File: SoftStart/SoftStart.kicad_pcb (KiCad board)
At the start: 2 copper layers, 88 x 56 mm, 31 parts, among them J1 LIVE, J10 LIVE, J11 Conn_01x02, J2 NEUTRAL, J3 SW1, J4 SW2, J5 NEUTRAL, J6 SWOUTPUT, J7 LIVE, J8 LIVE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

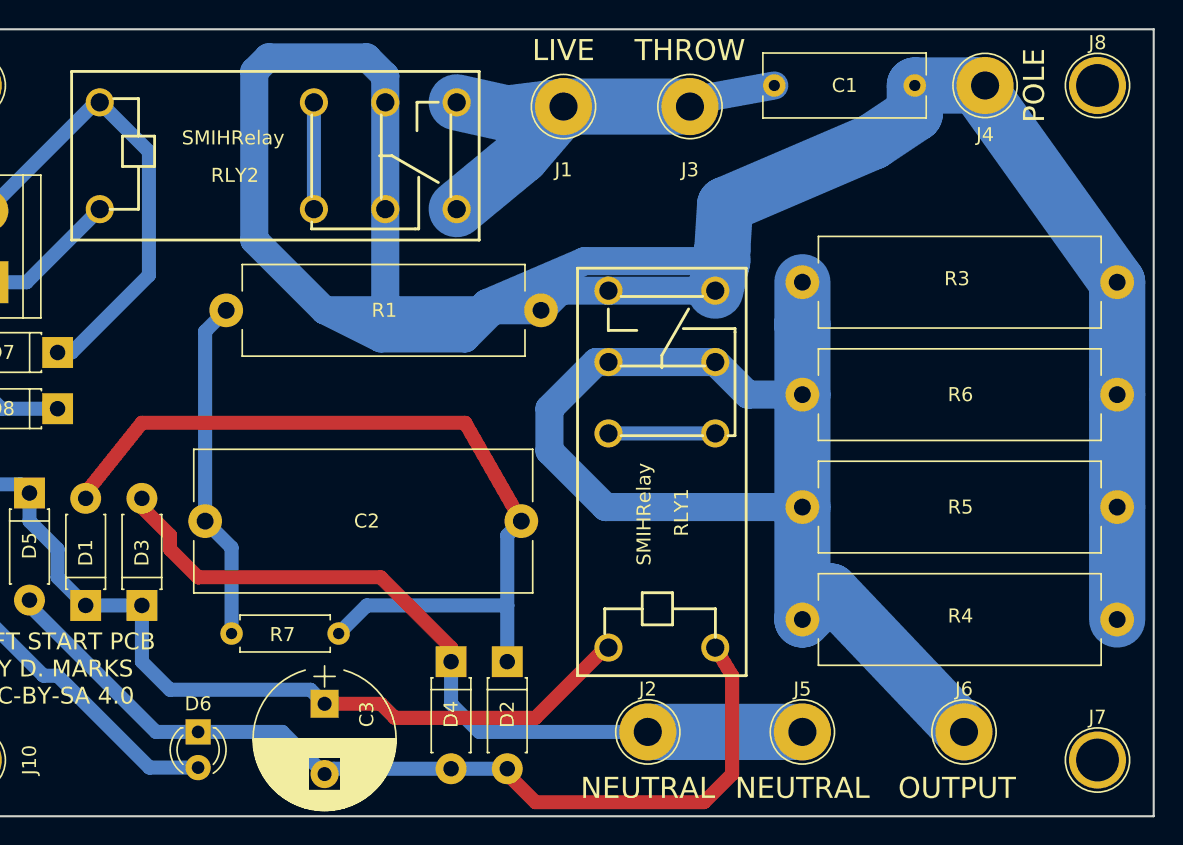
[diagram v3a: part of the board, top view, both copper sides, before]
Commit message: Changed to 2N5551/2N5401 from BC546C/BC556C transistors
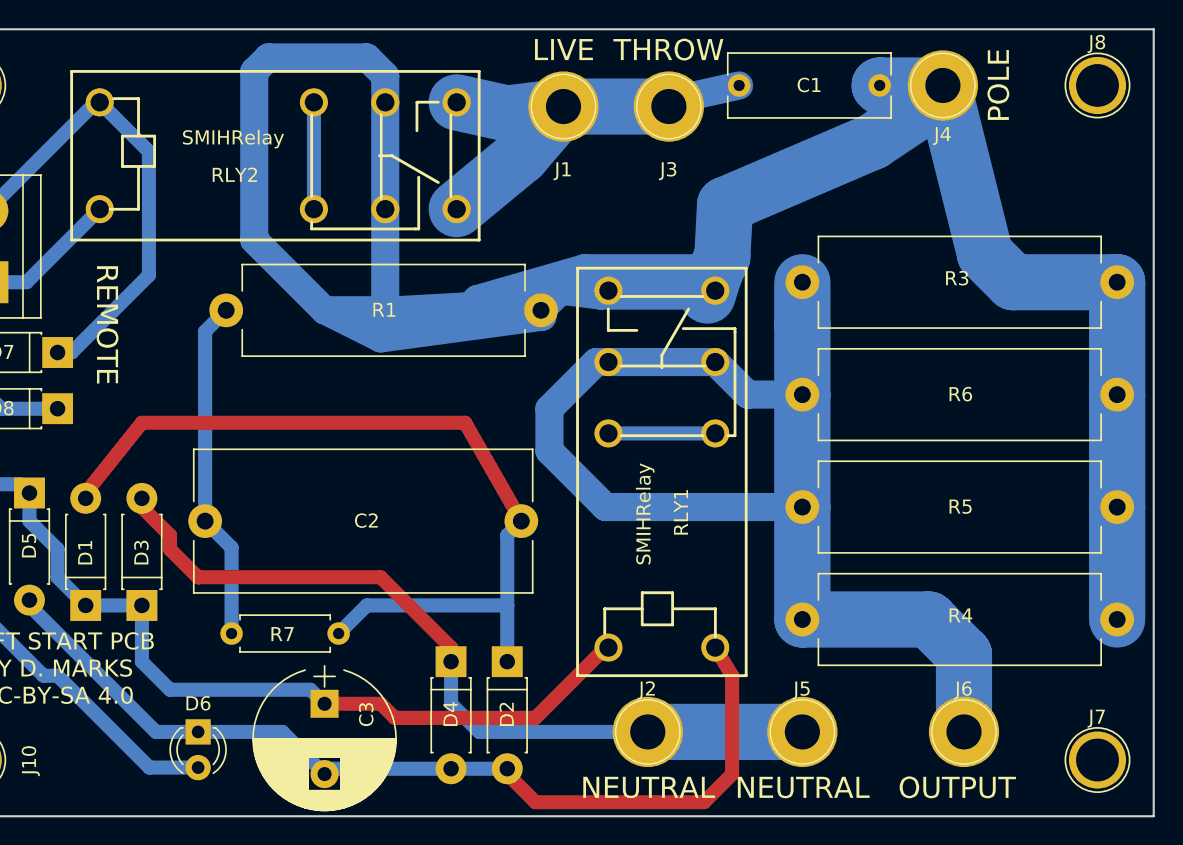
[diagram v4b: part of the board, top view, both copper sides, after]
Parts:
- moved J4 3.00 mm to (193.0, 73.0)
- moved C1 2.50 mm to (188.5, 73.0)
- moved J3 1.50 mm to (173.5, 74.5)
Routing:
- net Net-(C1-Pad1): track 179.0 -> 192.0 mm
- net Net-(C1-Pad2): track 33.6 -> 31.1 mm
- net Net-(J6-Pad1): track 83.6 -> 85.0 mm
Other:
- board text added: "REMOTE"
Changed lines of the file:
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@@
     (links 46)
     (no_connects 0)
-    (area 119.924999 68.924999 208.075001 125.075001)
+    (area 119.924999 68.465 208.075001 125.075001)
     (thickness 1.6)
-    (drawings 11)
-    (tracks 131)
+    (drawings 12)
+    (tracks 134)
     (zones 0)
     (modules 31)
@@
   )
   (setup
-    (last_trace_width 0.25)
+    (last_trace_width 2)
     (user_trace_width 0.5)
     (user_trace_width 1)
@@
     (mod_text_size 1 1)
     (mod_text_width 0.15)
-    (pad_size 4.064 4.064)
-    (pad_drill 2)
+    (pad_size 5 5)
+    (pad_drill 2.5)
     (pad_to_mask_clearance 0.2)
     (aux_axis_origin 0 0)
@@
   )
   (module Capacitors_THT:C_Rect_L11.5mm_W4.5mm_P10.00mm_MKT (layer F.Cu)
-    (at 191 73 180)
+    (at 188.5 73 180)
     (descr "C, Rect series, Radial, pin pitch=10.00mm, , length*width=11.5*4.5mm^2, Capacitor, https://en.tdk.eu/inf/20/20/db/fc_2009/MKT_B32560_564.pdf")
     (tags "C Rect series Radial pin pitch 10.00mm  length 11.5mm width 4.5mm Capacitor")
@@
     (fp_circle (center 0 0) (end 2.6 0) (layer F.CrtYd) (width 0.05))
     (fp_circle (center 0 0) (end 0 -2.286) (layer F.SilkS) (width 0.12))
-    (pad 1 thru_hole circle (at 0 0) (size 4.064 4.064) (drill 2) (layers *.Cu *.Mask)
+    (pad 1 thru_hole circle (at 0 0) (size 5 5) (drill 2.5) (layers *.Cu *.Mask)
       (net 2 "Net-(C1-Pad2)"))
   )
@@
     (fp_circle (center 0 0) (end 2.6 0) (layer F.CrtYd) (width 0.05))
     (fp_circle (center 0 0) (end 0 -2.286) (layer F.SilkS) (width 0.12))
-    (pad 1 thru_hole circle (at 0 0) (size 4.064 4.064) (drill 2) (layers *.Cu *.Mask)
+    (pad 1 thru_hole circle (at 0 0) (size 5 5) (drill 2.5) (layers *.Cu *.Mask)
       (net 7 "Net-(D3-Pad2)"))
   )
   (module Connectors:1pin (layer F.Cu)
-    (at 175 74.5)
+    (at 173.5 74.5)
     (descr "module 1 pin (ou trou mecanique de percage)")
     (tags DEV)
@@
     (fp_circle (center 0 0) (end 2.6 0) (layer F.CrtYd) (width 0.05))
     (fp_circle (center 0 0) (end 0 -2.286) (layer F.SilkS) (width 0.12))
-    (pad 1 thru_hole circle (at 0 0) (size 4.064 4.064) (drill 2) (layers *.Cu *.Mask)
+    (pad 1 thru_hole circle (at 0 0) (size 5 5) (drill 2.5) (layers *.Cu *.Mask)
       (net 2 "Net-(C1-Pad2)"))
   )
   (module Connectors:1pin (layer F.Cu)
-    (at 196 73)
+    (at 193 73)
     (descr "module 1 pin (ou trou mecanique de percage)")
     (tags DEV)
@@
     (fp_circle (center 0 0) (end 2.6 0) (layer F.CrtYd) (width 0.05))
     (fp_circle (center 0 0) (end 0 -2.286) (layer F.SilkS) (width 0.12))
-    (pad 1 thru_hole circle (at 0 0) (size 4.064 4.064) (drill 2) (layers *.Cu *.Mask)
+    (pad 1 thru_hole circle (at 0 0) (size 5 5) (drill 2.5) (layers *.Cu *.Mask)
       (net 1 "Net-(C1-Pad1)"))
   )
@@
     (fp_circle (center 0 0) (end 2.6 0) (layer F.CrtYd) (width 0.05))
     (fp_circle (center 0 0) (end 0 -2.286) (layer F.SilkS) (width 0.12))
-    (pad 1 thru_hole circle (at 0 0) (size 4.064 4.064) (drill 2) (layers *.Cu *.Mask)
+    (pad 1 thru_hole circle (at 0 0) (size 5 5) (drill 2.5) (layers *.Cu *.Mask)
       (net 7 "Net-(D3-Pad2)"))
   )
@@
     (fp_circle (center 0 0) (end 2.6 0) (layer F.CrtYd) (width 0.05))
     (fp_circle (center 0 0) (end 0 -2.286) (layer F.SilkS) (width 0.12))
-    (pad 1 thru_hole circle (at 0 0) (size 4.064 4.064) (drill 2) (layers *.Cu *.Mask)
+    (pad 1 thru_hole circle (at 0 0) (size 5 5) (drill 2.5) (layers *.Cu *.Mask)
       (net 9 "Net-(J6-Pad1)"))
   )
@@
       (net 2 "Net-(C1-Pad2)"))
   )
+  (gr_text REMOTE (at 133.5 90 270) (layer F.SilkS)
+    (effects (font (size 1.5 1.5) (thickness 0.3)))
+  )
   (gr_text "SOFT START PCB\nBY D. MARKS\nCC-BY-SA 4.0" (at 130 114.5) (layer F.SilkS)
     (effects (font (size 1.2 1.2) (thickness 0.2)))
@@
   (gr_line (start 208 69) (end 208 125) (angle 90) (layer Edge.Cuts) (width 0.15))
   (gr_line (start 120 69) (end 208 69) (angle 90) (layer Edge.Cuts) (width 0.15))
-  (gr_text POLE (at 199.5 73 90) (layer F.SilkS)
+  (gr_text POLE (at 197 73 90) (layer F.SilkS)
     (effects (font (size 1.5 1.5) (thickness 0.3)))
   )
-  (gr_text THROW (at 175 70.5) (layer F.SilkS)
+  (gr_text THROW (at 173.5 70.5) (layer F.SilkS)
     (effects (font (size 1.5 1.5) (thickness 0.3)))
   )
@@
     (effects (font (size 1.5 1.5) (thickness 0.3)))
   )
-  (segment (start 164.4 89) (end 161.5 88.5) (width 2) (layer B.Cu) (net 1))
+  (segment (start 205.4 87) (end 198 87) (width 4) (layer B.Cu) (net 1))
+  (segment (start 196 85) (end 193 73) (width 4) (layer B.Cu) (net 1) (status 20))
+  (segment (start 198 87) (end 196 85) (width 4) (layer B.Cu) (net 1))
+  (segment (start 164.4 89) (end 160.85 88.2) (width 2) (layer B.Cu) (net 1))
   (segment (start 153 91) (end 149 89) (width 2) (layer B.Cu) (net 1))
-  (segment (start 159 91) (end 153 91) (width 2) (layer B.Cu) (net 1))
-  (segment (start 161.5 88.5) (end 159 91) (width 2) (layer B.Cu) (net 1))
-  (segment (start 169.2 87.6) (end 176.8 87.6) (width 2) (layer B.Cu) (net 1))
+  (segment (start 164.5 89.45) (end 153 91) (width 2) (layer B.Cu) (net 1))
+  (segment (start 160.85 88.2) (end 164.5 89.45) (width 2) (layer B.Cu) (net 1))
+  (segment (start 168.65 87.95) (end 176.25 87.95) (width 2) (layer B.Cu) (net 1))
   (segment (start 153.32 81.8) (end 153.32 89) (width 2) (layer B.Cu) (net 1))
   (segment (start 153.32 89) (end 154 89) (width 2) (layer B.Cu) (net 1))
-  (segment (start 160 89) (end 160.5 88.5) (width 2) (layer B.Cu) (net 1))
-  (segment (start 167.5 85.5) (end 177.3 85.5) (width 2) (layer B.Cu) (net 1))
-  (segment (start 160.5 88.5) (end 167.5 85.5) (width 2) (layer B.Cu) (net 1))
-  (segment (start 169.2 87.6) (end 165.8 87.6) (width 2) (layer B.Cu) (net 1))
+  (segment (start 159.35 88.7) (end 159.85 88.2) (width 2) (layer B.Cu) (net 1))
+  (segment (start 167.5 86) (end 177.3 86) (width 2) (layer B.Cu) (net 1))
+  (segment (start 159.85 88.2) (end 167.5 86) (width 2) (layer B.Cu) (net 1))
+  (segment (start 168.65 87.95) (end 165.8 87.6) (width 2) (layer B.Cu) (net 1))
   (segment (start 165.8 87.6) (end 164.4 89) (width 2) (layer B.Cu) (net 1))
   (segment (start 153.32 74.2) (end 153.32 72.32) (width 2) (layer B.Cu) (net 1))
@@
   (segment (start 153.32 72.32) (end 152 71) (width 2) (layer B.Cu) (net 1))
   (segment (start 149 89) (end 154 89) (width 2) (layer B.Cu) (net 1))
-  (segment (start 154 89) (end 160 89) (width 2) (layer B.Cu) (net 1))
-  (segment (start 160 89) (end 164.4 89) (width 2) (layer B.Cu) (net 1))
+  (segment (start 154 89) (end 159.35 88.7) (width 2) (layer B.Cu) (net 1))
+  (segment (start 159.35 88.7) (end 164.4 89) (width 2) (layer B.Cu) (net 1))
   (segment (start 153.32 74.2) (end 153.32 81.8) (width 2) (layer B.Cu) (net 1) (status 30))
-  (segment (start 176.8 87.6) (end 177.3 85.5) (width 4) (layer B.Cu) (net 1) (status 10))
-  (segment (start 177.3 85.5) (end 177.3 84.7) (width 4) (layer B.Cu) (net 1) (status 10))
-  (segment (start 177.3 84.7) (end 177.5 81.5) (width 4) (layer B.Cu) (net 1))
+  (segment (start 176.25 87.95) (end 176.75 86.35) (width 4) (layer B.Cu) (net 1) (status 10))
+  (segment (start 176.75 86.35) (end 177.3 85.2) (width 4) (layer B.Cu) (net 1) (status 10))
+  (segment (start 177.3 85.2) (end 177.5 81.5) (width 4) (layer B.Cu) (net 1))
   (segment (start 177.5 81.5) (end 188 77) (width 4) (layer B.Cu) (net 1))
   (segment (start 188 77) (end 191 75) (width 4) (layer B.Cu) (net 1))
-  (segment (start 191 75) (end 191 73) (width 4) (layer B.Cu) (net 1) (status 20))
-  (segment (start 195 73) (end 191 73) (width 4) (layer B.Cu) (net 1) (status 10))
-  (segment (start 195 73) (end 195.4 73) (width 4) (layer B.Cu) (net 1) (status 30))
-  (segment (start 195.4 73) (end 205.4 87) (width 4) (layer B.Cu) (net 1) (status 10))
+  (segment (start 191 75) (end 188.5 73) (width 4) (layer B.Cu) (net 1) (status 20))
+  (segment (start 192 73) (end 188.5 73) (width 4) (layer B.Cu) (net 1) (status 20))
+  (segment (start 192 73) (end 192.4 73) (width 4) (layer B.Cu) (net 1) (status 30))
   (segment (start 205.4 103) (end 205.4 111) (width 4) (layer B.Cu) (net 1) (status 10))
   (segment (start 205.4 95) (end 205.4 103) (width 4) (layer B.Cu) (net 1) (status 10))
   (segment (start 205.4 87) (end 205.4 95) (width 4) (layer B.Cu) (net 1) (status 10))
-  (segment (start 175 74.5) (end 166 74.5) (width 4) (layer B.Cu) (net 2))
-  (segment (start 181 73) (end 175.5 74) (width 2) (layer B.Cu) (net 2) (status 10))
-  (segment (start 175.5 74) (end 175 74.5) (width 2) (layer B.Cu) (net 2))
+  (segment (start 173.5 74.5) (end 166 74.5) (width 4) (layer B.Cu) (net 2) (status 10))
+  (segment (start 178.5 73) (end 174 74) (width 2) (layer B.Cu) (net 2) (status 10))
+  (segment (start 174 74) (end 173.5 74.5) (width 2) (layer B.Cu) (net 2) (status 30))
   (segment (start 158.4 81.8) (end 163 78) (width 4) (layer B.Cu) (net 2) (status 10))
   (segment (start 163 78) (end 166 74.5) (width 4) (layer B.Cu) (net 2) (status 20))
@@
   (segment (start 129 115) (end 130 115) (width 1) (layer B.Cu) (net 8))
   (segment (start 124 110) (end 129 115) (width 1) (layer B.Cu) (net 8))
+  (segment (start 183 111) (end 192 111) (width 4) (layer B.Cu) (net 9))
+  (segment (start 194.5 113.5) (end 194.5 119) (width 4) (layer B.Cu) (net 9))
+  (segment (start 192 111) (end 194.5 113.5) (width 4) (layer B.Cu) (net 9))
   (segment (start 169.2 92.68) (end 168.32 92.68) (width 2) (layer B.Cu) (net 9))
   (segment (start 168.32 92.68) (end 165 96) (width 2) (layer B.Cu) (net 9))
@@
   (segment (start 183 90) (end 183 95) (width 4) (layer B.Cu) (net 9) (status 20))
   (segment (start 183 103) (end 183 111) (width 4) (layer B.Cu) (net 9) (status 10))
-  (segment (start 183 111) (end 185 109) (width 4) (layer B.Cu) (net 9) (status 10))
-  (segment (start 185 109) (end 194.5 119) (width 4) (layer B.Cu) (net 9) (status 20))
   (segment (start 176.8 97.76) (end 169.2 97.76) (width 1) (layer B.Cu) (net 10))
   (segment (start 133 74.2) (end 132.72 74.2) (width 1) (layer B.Cu) (net 11))

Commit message: Working design 2020-10-12
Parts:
- added J12: NEUTRAL, Connectors:1pin, F.Cu at (188.0, 80.0)
- added J13: NEUTRAL, Connectors:1pin, F.Cu at (199.0, 80.0)
- added J14: NEUTRAL, Connectors:1pin, F.Cu at (205.0, 80.0)
- added J15: NEUTRAL, Connectors:1pin, F.Cu at (186.0, 120.0)
- added J16: NEUTRAL, Connectors:1pin, F.Cu at (198.0, 120.0)
- added J17: NEUTRAL, Connectors:1pin, F.Cu at (165.0, 120.0)
- moved C3 8.00 mm to (141.0, 117.0)
- moved D6 8.00 mm to (132.0, 119.0)
- moved D2 4.47 mm to (158.0, 112.0)
- moved D4 4.47 mm to (154.0, 112.0)
- moved J5 3.16 mm to (180.0, 120.0)
- moved J6 2.69 mm to (192.0, 120.0)
- moved RLY1 2.00 mm to (173.0, 101.0)
- moved J2 1.00 mm to (172.0, 120.0)
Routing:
- net Net-(C1-Pad1): track 192.0 -> 223.1 mm
- net Net-(D6-Pad2): track 21.8 -> 17.3 mm
- net Net-(C3-Pad2): track 66.8 -> 62.8 mm
- net Net-(C2-Pad1): track 61.1 -> 64.2 mm
- net Net-(D3-Pad2): track 57.4 -> 58.5 mm
- net Net-(J6-Pad1): track 85.0 -> 85.9 mm

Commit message: Changed components for lower quiescent power
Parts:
- added JP1: Jumper_NC_Small, Pin_Headers:Pin_Header_Straight_1x02_Pitch2.54mm, F.Cu at (145.0, 111.7)
- moved R7 16.4 mm to (156.7, 97.0)
- moved C3 3.00 mm to (141.0, 120.0), turned to 0 degrees
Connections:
- D1 pad 1: Net-(C3-Pad1) -> Net-(D1-Pad1)
- D3 pad 1: Net-(C3-Pad1) -> Net-(D1-Pad1)
- D5 pad 1: Net-(C3-Pad1) -> Net-(D1-Pad1)
- R2 pad 2: Net-(C3-Pad1) -> Net-(D1-Pad1)
- RLY1 pad 4: Net-(C3-Pad1) -> Net-(D1-Pad1)
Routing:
- net Net-(D1-Pad1): track 0.00 -> 62.7 mm
- net Net-(C3-Pad1): track 59.0 -> 9.10 mm
- net Net-(C2-Pad1): track 64.2 -> 52.3 mm
- net Net-(D3-Pad2): track 58.5 -> 56.6 mm
- net Net-(C3-Pad2): track 62.8 -> 64.2 mm

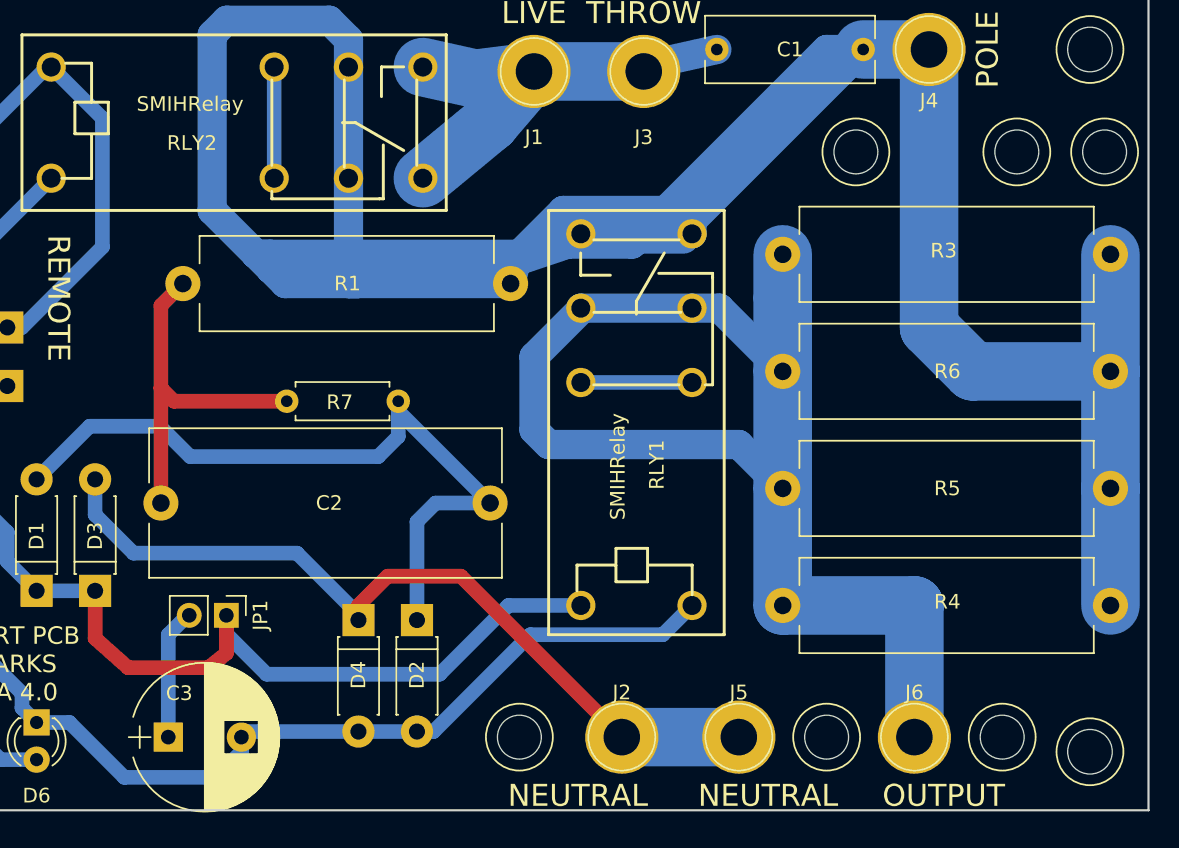
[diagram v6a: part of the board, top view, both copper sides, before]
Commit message: Modified soft start to have wire jumper over resistors
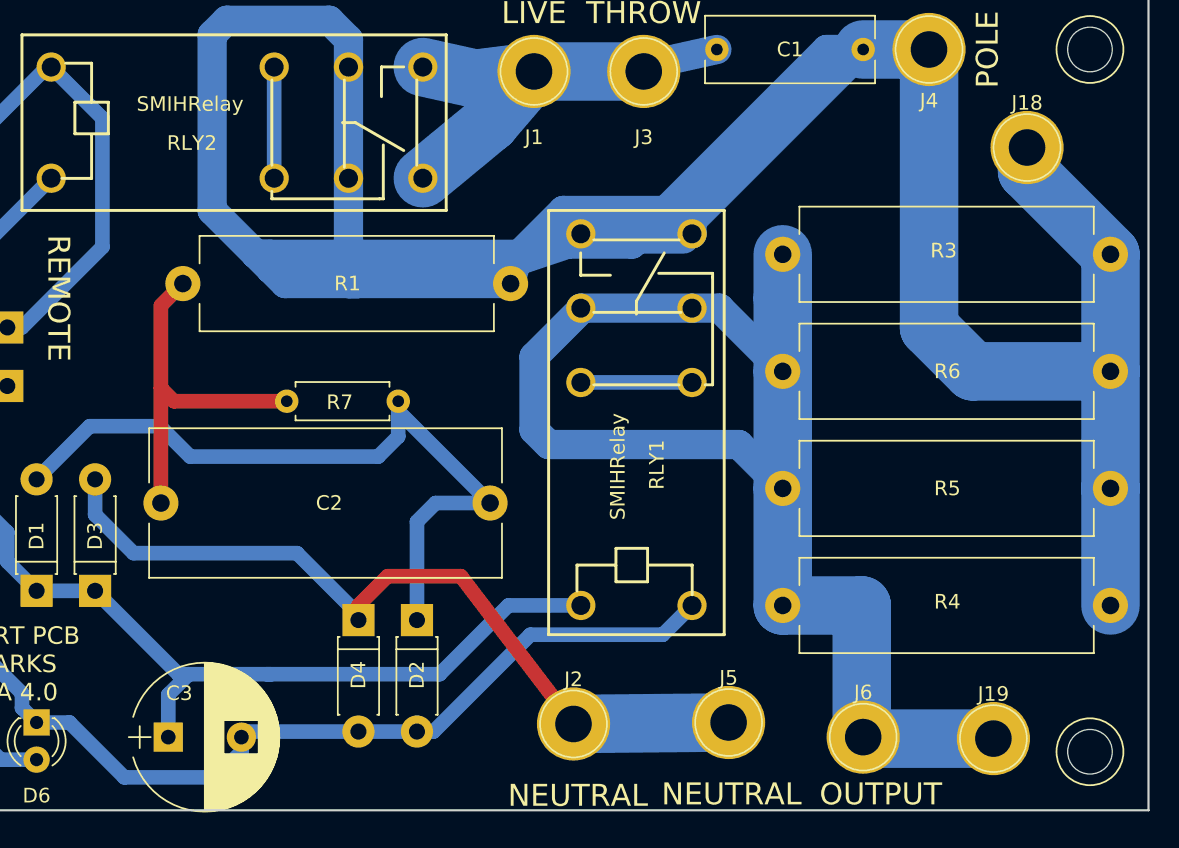
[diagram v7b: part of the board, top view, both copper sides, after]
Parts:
- removed J12, J13, J14, J15, J16, J17: NEUTRAL, Connectors:1pin
- removed JP1: Jumper_NC_Small, Pin_Headers:Pin_Header_Straight_1x02_Pitch2.54mm
- added J18: SW2, Connectors:1pin, F.Cu at (199.7, 79.7)
- added J19: SW2, Connectors:1pin, F.Cu at (197.4, 120.1)
- moved J6 3.50 mm to (188.5, 120.0)
- moved J2 3.42 mm to (168.7, 119.1)
- moved J5 1.22 mm to (179.3, 119.0)
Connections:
- D1 pad 1: Net-(D1-Pad1) -> Net-(C3-Pad1)
- D3 pad 1: Net-(D1-Pad1) -> Net-(C3-Pad1)
- D5 pad 1: Net-(D1-Pad1) -> Net-(C3-Pad1)
- R2 pad 2: Net-(D1-Pad1) -> Net-(C3-Pad1)
- RLY1 pad 4: Net-(D1-Pad1) -> Net-(C3-Pad1)
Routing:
- net Net-(D1-Pad1): track 62.7 -> 0.00 mm
- net Net-(C3-Pad1): track 9.10 -> 60.9 mm
- net Net-(C1-Pad1): track 223.1 -> 232.7 mm
- net Net-(J19-Pad1): track 85.9 -> 91.2 mm
